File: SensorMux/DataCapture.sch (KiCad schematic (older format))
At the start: 40 parts

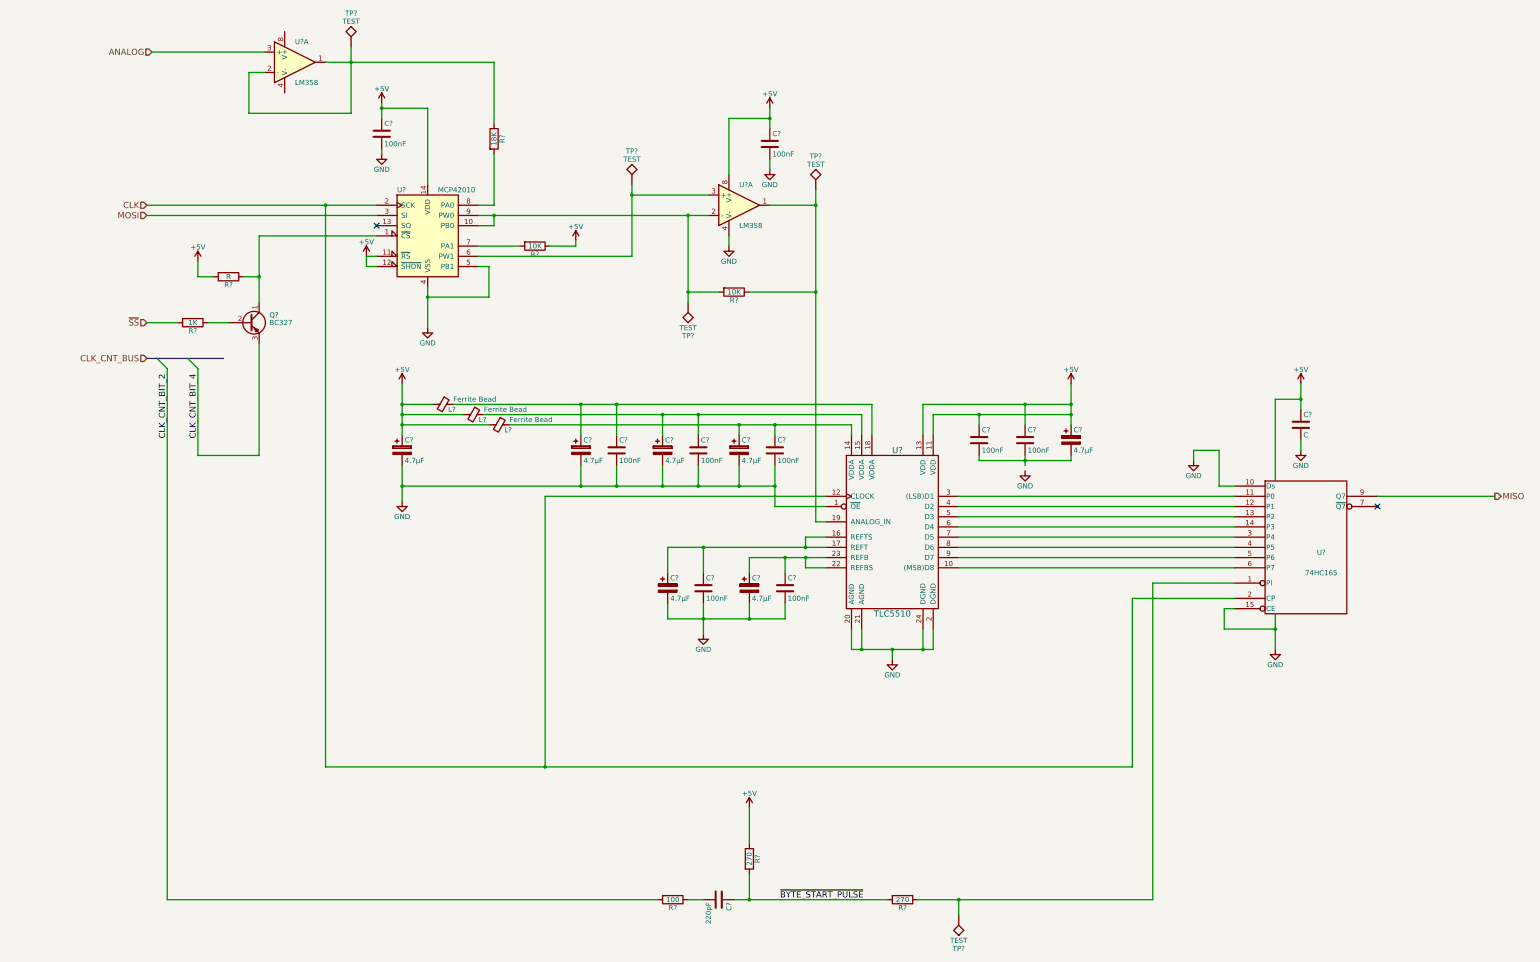
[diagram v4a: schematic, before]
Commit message: Working on new connector grid.
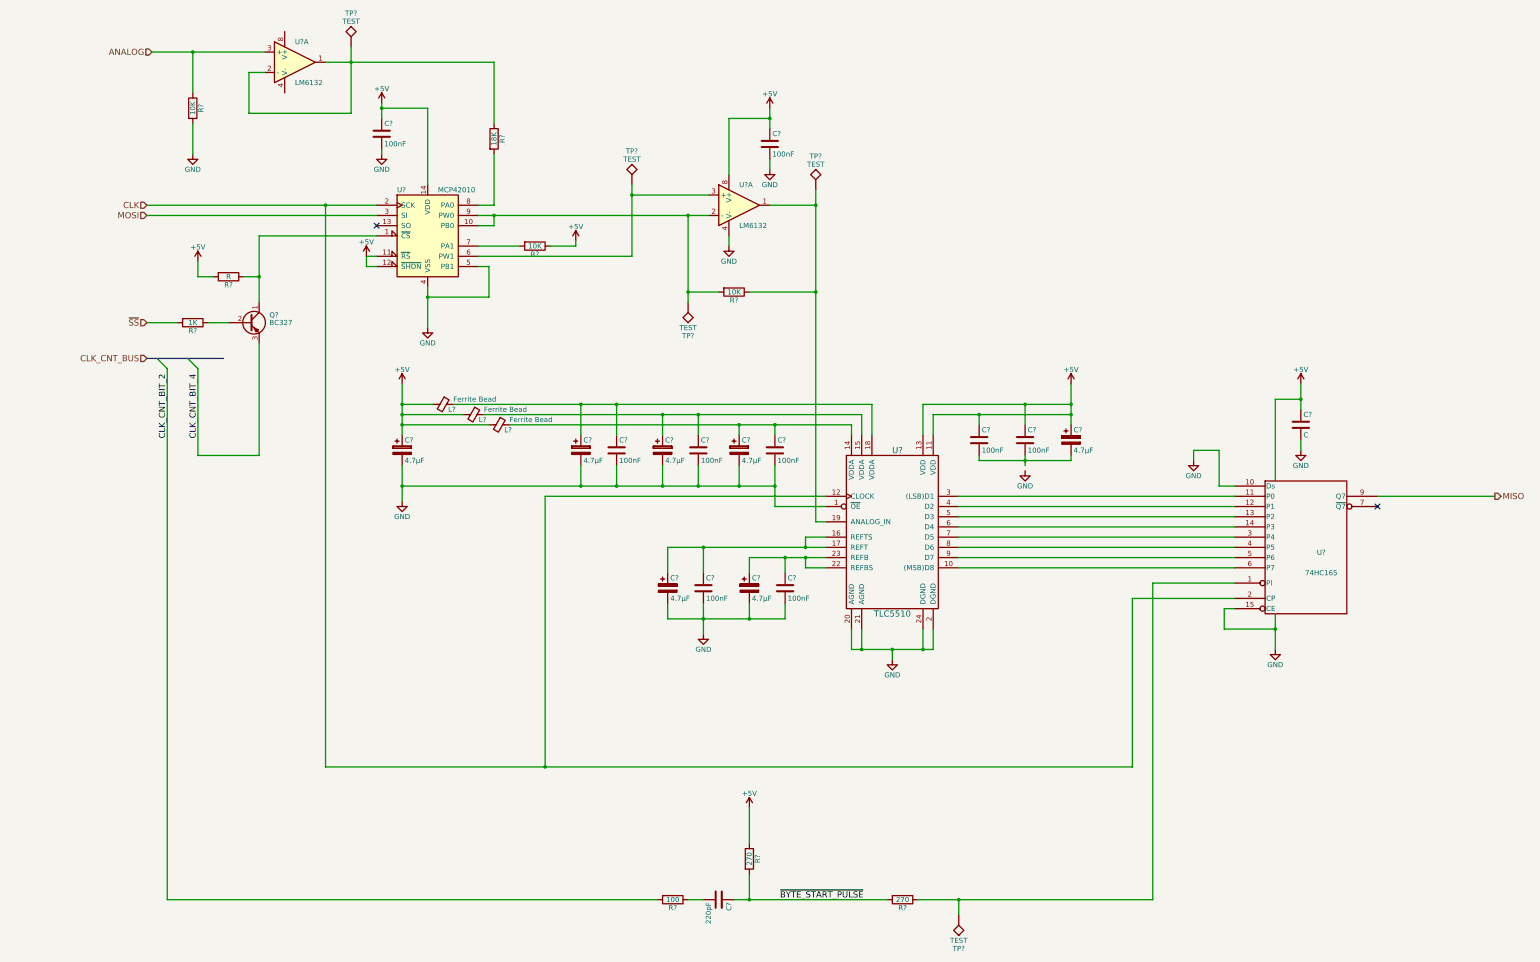
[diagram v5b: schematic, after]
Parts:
- added R?: 10K, symbol R
- U? (x2): value LM358 -> LM6132
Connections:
- net ANALOG: now also R?.1
- net GND: now also R?.2
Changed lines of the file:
@@
 P 7700 3050
 F 0 "U?" H 7700 3250 50  0000 L CNN
-F 1 "LM358" H 7700 2850 50  0000 L CNN
+F 1 "LM6132" H 7700 2850 50  0000 L CNN
 F 2 "" H 7700 3050 50  0001 C CNN
 F 3 "" H 7700 3050 50  0001 C CNN
@@
 P 3350 1650
 F 0 "U?" H 3350 1850 50  0000 L CNN
-F 1 "LM358" H 3350 1450 50  0000 L CNN
+F 1 "LM6132" H 3350 1450 50  0000 L CNN
 F 2 "" H 3350 1650 50  0001 C CNN
 F 3 "" H 3350 1650 50  0001 C CNN
@@
 	13950 5900 15100 5900
 Wire Wire Line
-	12950 7050 12950 7200
-Wire Wire Line
-	12950 7200 12950 7400
+	12950 7050 12950 7400
 Wire Wire Line
 	12450 7200 12950 7200
@@
 	12950 4950 13200 4950
 Wire Wire Line
-	13200 4800 13200 4950
-Wire Wire Line
-	13200 4950 13200 5050
+	13200 4800 13200 5050
 Connection ~ 13200 4950
 Wire Wire Line
 	13200 5350 13200 5450
 Wire Wire Line
-	11750 9850 9850 9850
-Wire Wire Line
-	9850 9850 9450 9850
-Wire Wire Line
-	7650 9850 7800 9850
-Wire Wire Line
-	7800 9850 9150 9850
-Wire Wire Line
-	3650 8550 5800 8550
-Wire Wire Line
-	5800 8550 11550 8550
+	11750 9850 9450 9850
+Wire Wire Line
+	7650 9850 9150 9850
+Wire Wire Line
+	3650 8550 11550 8550
 Wire Wire Line
 	11550 8550 11550 6900
@@
 	8800 5200 8800 5300
 Wire Wire Line
-	5450 5200 7700 5200
-Wire Wire Line
-	7700 5200 8050 5200
-Wire Wire Line
-	8050 5200 8800 5200
+	5450 5200 8800 5200
 Wire Wire Line
 	8900 5100 8900 5300
 Wire Wire Line
-	5200 5100 6950 5100
-Wire Wire Line
-	6950 5100 7300 5100
-Wire Wire Line
-	7300 5100 8900 5100
+	5200 5100 8900 5100
 Wire Wire Line
 	9000 5000 9000 5300
 Wire Wire Line
-	4900 5000 6150 5000
-Wire Wire Line
-	6150 5000 6500 5000
-Wire Wire Line
-	6500 5000 9000 5000
+	4900 5000 9000 5000
 Wire Wire Line
 	4400 5000 4700 5000
 Wire Wire Line
-	8050 5600 8050 5800
-Wire Wire Line
-	8050 5800 8050 6000
+	8050 5600 8050 6000
 Wire Wire Line
 	7700 5800 7700 5600
@@
 	6150 5600 6150 5800
 Wire Wire Line
-	4400 5800 6150 5800
-Wire Wire Line
-	6150 5800 6500 5800
-Wire Wire Line
-	6500 5800 6950 5800
-Wire Wire Line
-	6950 5800 7300 5800
-Wire Wire Line
-	7300 5800 7700 5800
-Wire Wire Line
-	7700 5800 8050 5800
+	4400 5800 8050 5800
 Wire Wire Line
 	4400 5200 5250 5200
 Wire Wire Line
-	4400 4800 4400 5000
-Wire Wire Line
-	4400 5000 4400 5100
-Wire Wire Line
-	4400 5100 4400 5200
-Wire Wire Line
-	4400 5200 4400 5300
+	4400 4800 4400 5300
 Wire Wire Line
 	4400 5100 5000 5100
@@
 	8050 6000 8550 6000
 Wire Wire Line
-	4400 5600 4400 5800
-Wire Wire Line
-	4400 5800 4400 5950
+	4400 5600 4400 5950
 Connection ~ 6150 5800
 Connection ~ 4400 5800
@@
 	8550 6300 8350 6300
 Wire Wire Line
-	7000 6400 7350 6400
-Wire Wire Line
-	7350 6400 8350 6400
-Wire Wire Line
-	8350 6400 8550 6400
+	7000 6400 8550 6400
 Wire Wire Line
 	8350 6600 8550 6600
@@
 	8350 6500 8350 6600
 Wire Wire Line
-	7800 6500 8150 6500
-Wire Wire Line
-	8150 6500 8350 6500
-Wire Wire Line
-	8350 6500 8550 6500
+	7800 6500 8550 6500
 Connection ~ 8350 6500
 Wire Wire Line
@@
 	7000 6950 7000 7100
 Wire Wire Line
-	7000 7100 7350 7100
-Wire Wire Line
-	7350 7100 7800 7100
-Wire Wire Line
-	7800 7100 8150 7100
+	7000 7100 8150 7100
 Wire Wire Line
 	8150 7100 8150 6950
 Wire Wire Line
-	7350 6950 7350 7100
-Wire Wire Line
-	7350 7100 7350 7250
+	7350 6950 7350 7250
 Connection ~ 7350 7100
 Wire Wire Line
@@
 	8900 7200 8900 7400
 Wire Wire Line
-	8800 7400 8900 7400
-Wire Wire Line
-	8900 7400 9200 7400
-Wire Wire Line
-	9200 7400 9500 7400
-Wire Wire Line
-	9500 7400 9600 7400
+	8800 7400 9600 7400
 Wire Wire Line
 	9200 7400 9200 7500
@@
 	9600 5300 9600 5100
 Wire Wire Line
-	9600 5100 10050 5100
-Wire Wire Line
-	10050 5100 10950 5100
-Wire Wire Line
-	10950 4800 10950 5000
-Wire Wire Line
-	10950 5000 10950 5100
-Wire Wire Line
-	10950 5100 10950 5200
+	9600 5100 10950 5100
+Wire Wire Line
+	10950 4800 10950 5200
 Wire Wire Line
 	9500 5300 9500 5000
 Wire Wire Line
-	9500 5000 10500 5000
-Wire Wire Line
-	10500 5000 10950 5000
+	9500 5000 10950 5000
 Connection ~ 10950 5100
 Wire Wire Line
@@
 	10050 5500 10050 5550
 Wire Wire Line
-	10050 5550 10500 5550
-Wire Wire Line
-	10500 5550 10950 5550
-Wire Wire Line
-	10500 5500 10500 5550
-Wire Wire Line
-	10500 5550 10500 5600
+	10050 5550 10950 5550
+Wire Wire Line
+	10500 5500 10500 5600
 Wire Wire Line
 	10950 5550 10950 5500
@@
 	2900 1750 2900 2150
 Wire Wire Line
-	3900 1500 3900 1650
-Wire Wire Line
-	3900 1650 3900 2150
-Wire Wire Line
-	3650 1650 3900 1650
-Wire Wire Line
-	3900 1650 5300 1650
+	3900 1500 3900 2150
+Wire Wire Line
+	3650 1650 5300 1650
 Connection ~ 3900 1650
 Wire Wire Line
@@
 	3900 2150 2900 2150
 Wire Wire Line
-	4650 3850 4650 3950
-Wire Wire Line
-	4650 3950 4650 4250
+	4650 3850 4650 4250
 Connection ~ 4650 3950
 Wire Wire Line
-	4200 2050 4200 2100
-Wire Wire Line
-	4200 2100 4200 2200
+	4200 2050 4200 2200
 Wire Wire Line
 	4200 2100 4650 2100
@@
 	4200 2500 4200 2550
 Wire Wire Line
-	1900 3050 3650 3050
-Wire Wire Line
-	3650 3050 4150 3050
+	1900 3050 4150 3050
 Wire Wire Line
 	1900 3150 4150 3150
 Wire Bus Line
-	1900 4550 2000 4550
-Wire Bus Line
-	2000 4550 2300 4550
-Wire Bus Line
-	2300 4550 2650 4550
+	1900 4550 2650 4550
 Wire Wire Line
 	4150 3550 4050 3550
@@
 	5300 1650 5300 2250
 Wire Wire Line
-	5150 3150 5300 3150
-Wire Wire Line
-	5300 3150 7200 3150
-Wire Wire Line
-	7200 3150 7400 3150
-Wire Wire Line
-	7200 3150 7200 3900
-Wire Wire Line
-	7200 3900 7200 4000
+	5150 3150 7400 3150
+Wire Wire Line
+	7200 3150 7200 4000
 Wire Wire Line
 	7200 3900 7500 3900
@@
 	8450 3900 7800 3900
 Wire Wire Line
-	8450 2900 8450 3050
-Wire Wire Line
-	8450 3050 8450 3900
-Wire Wire Line
-	8450 3900 8450 6150
+	8450 2900 8450 6150
 Wire Wire Line
 	8450 3050 8000 3050
@@
 	6650 3550 5150 3550
 Wire Wire Line
-	6650 2850 6650 2950
-Wire Wire Line
-	6650 2950 6650 3550
+	6650 2850 6650 3550
 Wire Wire Line
 	6650 2950 7400 2950
@@
 	7600 2200 8000 2200
 Wire Wire Line
-	8000 2100 8000 2200
-Wire Wire Line
-	8000 2200 8000 2300
+	8000 2100 8000 2300
 Connection ~ 8000 2200
 Wire Wire Line
@@
 	3000 5500 3000 4400
 Wire Wire Line
-	3000 4000 3000 3750
-Wire Wire Line
-	3000 3750 3000 3350
+	3000 3350 3000 4000
 Wire Wire Line
 	3000 3350 4150 3350
@@
 	3650 8550 3650 3050
 Connection ~ 3650 3050
+Wire Wire Line
+	2350 1550 2350 1950
+Connection ~ 2350 1550
+$Comp
+L R R?
+U 1 1 5A6E0A6F
+P 2350 2100
+F 0 "R?" V 2430 2100 50  0000 C CNN
+F 1 "10K" V 2350 2100 50  0000 C CNN
+F 2 "" V 2280 2100 50  0001 C CNN
+F 3 "" H 2350 2100 50  0001 C CNN
+	1    2350 2100
+	1    0    0    -1
+$EndComp
+Wire Wire Line
+	2350 2250 2350 2550
+$Comp
+L GND #PWR?
+U 1 1 5A6E0C2E
+P 2350 2550
+F 0 "#PWR?" H 2350 2300 50  0001 C CNN
+F 1 "GND" H 2350 2400 50  0000 C CNN
+F 2 "" H 2350 2550 50  0001 C CNN
+F 3 "" H 2350 2550 50  0001 C CNN
+	1    2350 2550
+	1    0    0    -1
+$EndComp
 $EndSCHEMATC
